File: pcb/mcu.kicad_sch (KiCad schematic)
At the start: 33 parts, among them J1 Conn_01x02_Pin, SW2 SW_Push, U1 TLV1117LV33DCYR, U2 W25Q64JVSSIQ_C179171, U3 STM32H750VBTx, Y1 25 MHz

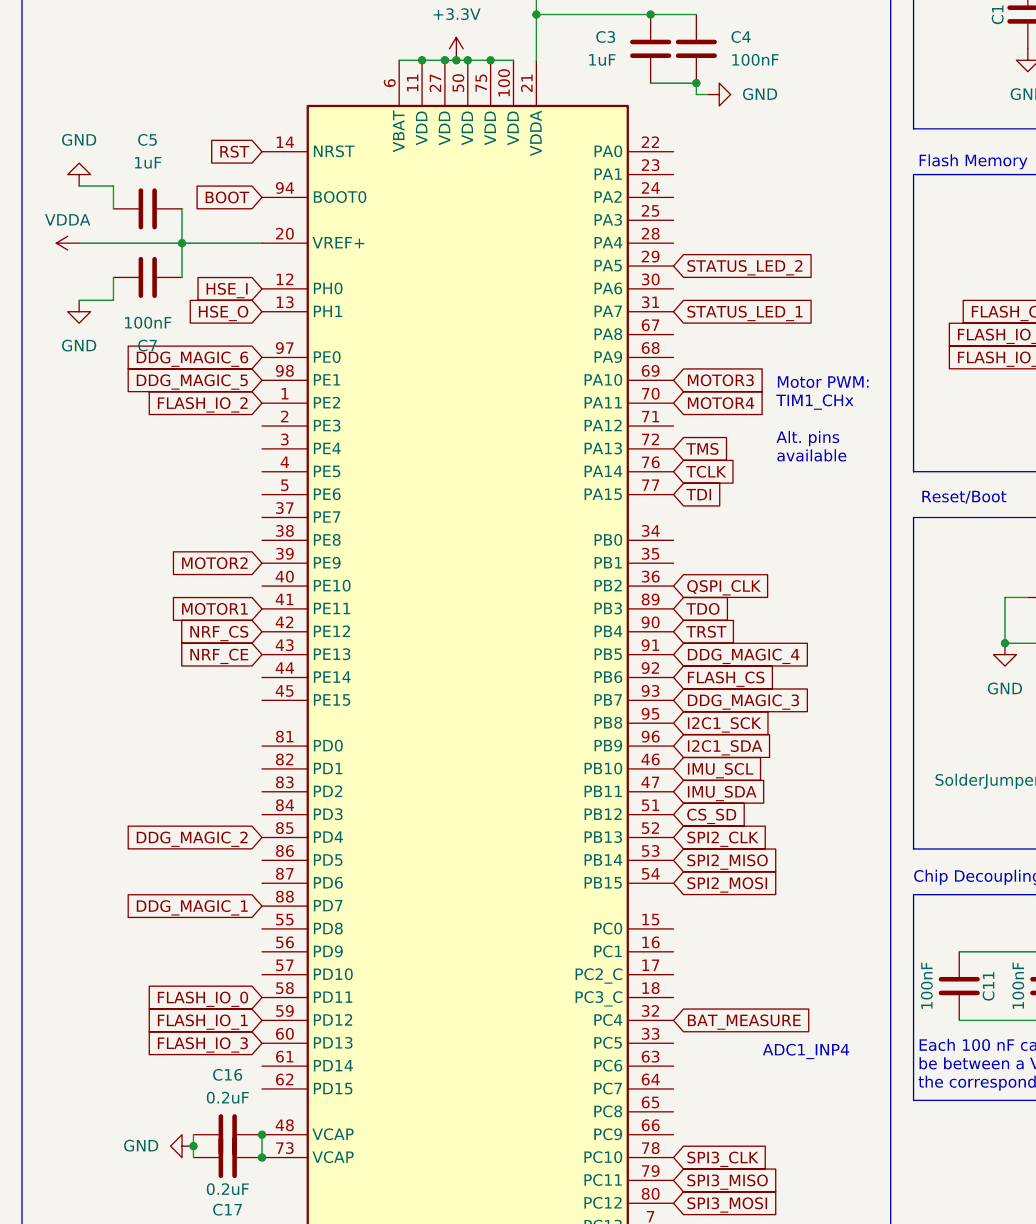
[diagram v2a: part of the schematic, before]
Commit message: [pcb] utilize unused gpios, silkscreen improvements and [journal] add entry for 7/9
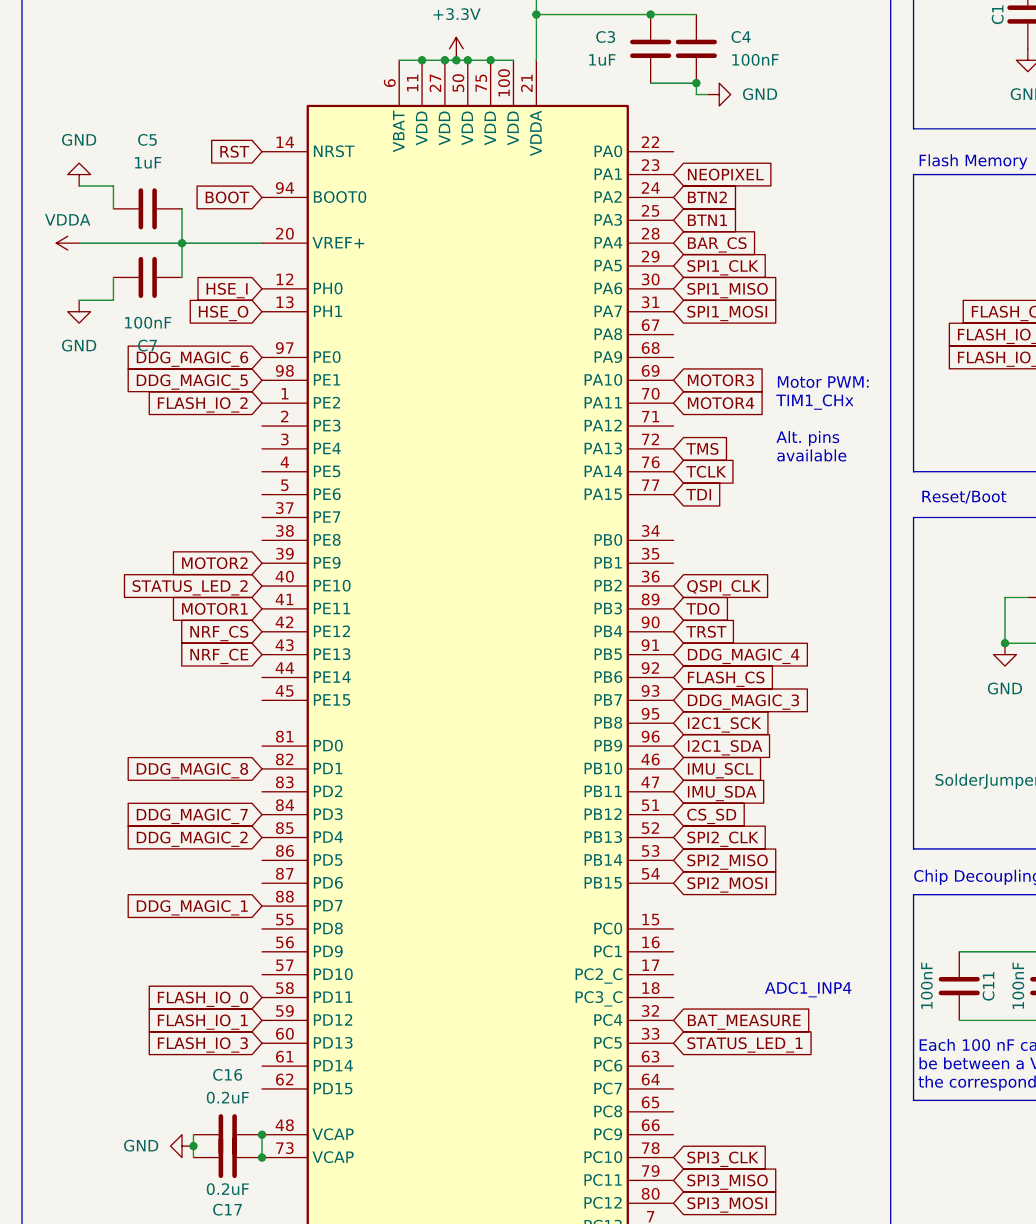
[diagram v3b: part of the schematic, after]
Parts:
- SW2: footprint Button_Switch_THT:SW_PUSH_6mm -> lcsc:SW-SMD_L4.0-W2.9-LS5.0
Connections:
- net STATUS_LED_1: now also U3.33 (PC5); no longer U3.31 (PA7)
- net STATUS_LED_2: now also U3.40 (PE10); no longer U3.29 (PA5)
- net NEOPIXEL: now reaches U3.23 (PA1)
- net BTN2: now reaches U3.24 (PA2)
- net BTN1: now reaches U3.25 (PA3)
- net BAR_CS: now reaches U3.28 (PA4)
- net SPI1_MISO: now reaches U3.30 (PA6)
- net DDG_MAGIC_8: now reaches U3.82 (PD1)
- net DDG_MAGIC_7: now reaches U3.84 (PD3)
- new net SPI1_CLK: U3.29 (PA5)
- new net SPI1_MOSI: U3.31 (PA7)
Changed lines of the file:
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@@
 	(text "ADC1_INP4"
 		(exclude_from_sim no)
-		(at 97.536 145.796 0)
+		(at 97.79 138.938 0)
 		(effects
 			(font
@@
 		)
 	)
+	(global_label "SPI1_CLK"
+		(shape input)
+		(at 87.63 58.42 0)
+		(fields_autoplaced yes)
+		(effects
+			(font
+				(size 1.27 1.27)
+			)
+			(justify left)
+		)
+		(property "Intersheetrefs" "${INTERSHEET_REFS}"
+			(at 99.4447 58.42 0)
+			(effects
+				(font
+					(size 1.27 1.27)
+				)
+				(justify left)
+				(hide yes)
+			)
+		)
+	)
 	(global_label "I2C1_SDA"
 		(shape input)
@@
 		)
 	)
+	(global_label "STATUS_LED_2"
+		(shape input)
+		(at 41.91 93.98 180)
+		(fields_autoplaced yes)
+		(effects
+			(font
+				(size 1.27 1.27)
+			)
+			(justify right)
+		)
+		(property "Intersheetrefs" "${INTERSHEET_REFS}"
+			(at 25.5597 93.98 0)
+			(effects
+				(font
+					(size 1.27 1.27)
+				)
+				(justify right)
+				(hide yes)
+			)
+		)
+	)
 	(global_label "TMS"
 		(shape input)
@@
 		)
 	)
+	(global_label "BAR_CS"
+		(shape input)
+		(at 87.63 55.88 0)
+		(fields_autoplaced yes)
+		(effects
+			(font
+				(size 1.27 1.27)
+			)
+			(justify left)
+		)
+		(property "Intersheetrefs" "${INTERSHEET_REFS}"
+			(at 97.6909 55.88 0)
+			(effects
+				(font
+					(size 1.27 1.27)
+				)
+				(justify left)
+				(hide yes)
+			)
+		)
+	)
 	(global_label "HSE_O"
 		(shape input)
@@
 		)
 	)
+	(global_label "SPI1_MISO"
+		(shape input)
+		(at 87.63 60.96 0)
+		(fields_autoplaced yes)
+		(effects
+			(font
+				(size 1.27 1.27)
+			)
+			(justify left)
+		)
+		(property "Intersheetrefs" "${INTERSHEET_REFS}"
+			(at 100.4728 60.96 0)
+			(effects
+				(font
+					(size 1.27 1.27)
+				)
+				(justify left)
+				(hide yes)
+			)
+		)
+	)
 	(global_label "SPI2_CLK"
 		(shape input)
@@
 		)
 	)
+	(global_label "STATUS_LED_1"
+		(shape input)
+		(at 87.63 144.78 0)
+		(fields_autoplaced yes)
+		(effects
+			(font
+				(size 1.27 1.27)
+			)
+			(justify left)
+		)
+		(property "Intersheetrefs" "${INTERSHEET_REFS}"
+			(at 103.9803 144.78 0)
+			(effects
+				(font
+					(size 1.27 1.27)
+				)
+				(justify left)
+				(hide yes)
+			)
+		)
+	)
 	(global_label "SPI3_MISO"
 		(shape input)
@@
 		)
 	)
-	(global_label "STATUS_LED_1"
+	(global_label "BTN2"
 		(shape input)
-		(at 87.63 63.5 0)
+		(at 87.63 50.8 0)
 		(fields_autoplaced yes)
 		(effects
@@
 		)
 		(property "Intersheetrefs" "${INTERSHEET_REFS}"
-			(at 103.9803 63.5 0)
+			(at 95.3928 50.8 0)
+			(effects
+				(font
+					(size 1.27 1.27)
+				)
+				(justify left)
+				(hide yes)
+			)
+		)
+	)
+	(global_label "NEOPIXEL"
+		(shape input)
+		(at 87.63 48.26 0)
+		(fields_autoplaced yes)
+		(effects
+			(font
+				(size 1.27 1.27)
+			)
+			(justify left)
+		)
+		(property "Intersheetrefs" "${INTERSHEET_REFS}"
+			(at 99.6866 48.26 0)
 			(effects
 				(font
@@
 		)
 	)
+	(global_label "DDG_MAGIC_8"
+		(shape input)
+		(at 41.91 114.3 180)
+		(fields_autoplaced yes)
+		(effects
+			(font
+				(size 1.27 1.27)
+			)
+			(justify right)
+		)
+		(property "Intersheetrefs" "${INTERSHEET_REFS}"
+			(at 26.2853 114.3 0)
+			(effects
+				(font
+					(size 1.27 1.27)
+				)
+				(justify right)
+				(hide yes)
+			)
+		)
+	)
 	(global_label "RST"
 		(shape input)
@@
 		)
 	)
-	(global_label "STATUS_LED_2"
+	(global_label "DDG_MAGIC_7"
 		(shape input)
-		(at 87.63 58.42 0)
+		(at 41.91 119.38 180)
+		(fields_autoplaced yes)
+		(effects
+			(font
+				(size 1.27 1.27)
+			)
+			(justify right)
+		)
+		(property "Intersheetrefs" "${INTERSHEET_REFS}"
+			(at 26.2853 119.38 0)
+			(effects
+				(font
+					(size 1.27 1.27)
+				)
+				(justify right)
+				(hide yes)
+			)
+		)
+	)
+	(global_label "SPI1_MOSI"
+		(shape input)
+		(at 87.63 63.5 0)
 		(fields_autoplaced yes)
 		(effects
@@
 		)
 		(property "Intersheetrefs" "${INTERSHEET_REFS}"
-			(at 103.9803 58.42 0)
+			(at 100.4728 63.5 0)
 			(effects
 				(font
@@
 		)
 	)
+	(global_label "BTN1"
+		(shape input)
+		(at 87.63 53.34 0)
+		(fields_autoplaced yes)
+		(effects
+			(font
+				(size 1.27 1.27)
+			)
+			(justify left)
+		)
+		(property "Intersheetrefs" "${INTERSHEET_REFS}"
+			(at 95.3928 53.34 0)
+			(effects
+				(font
+					(size 1.27 1.27)
+				)
+				(justify left)
+				(hide yes)
+			)
+		)
+	)
 	(global_label "I2C1_SCK"
 		(shape input)
@@
 			)
 		)
-		(property "Footprint" "Button_Switch_THT:SW_PUSH_6mm"
+		(property "Footprint" "lcsc:SW-SMD_L4.0-W2.9-LS5.0"
 			(at 132.08 90.17 0)
 			(effects
@@
 		(on_board yes)
 		(dnp no)
-		(fields_autoplaced yes)
 		(property "Reference" "U3"
 			(at 69.4533 177.8 0)

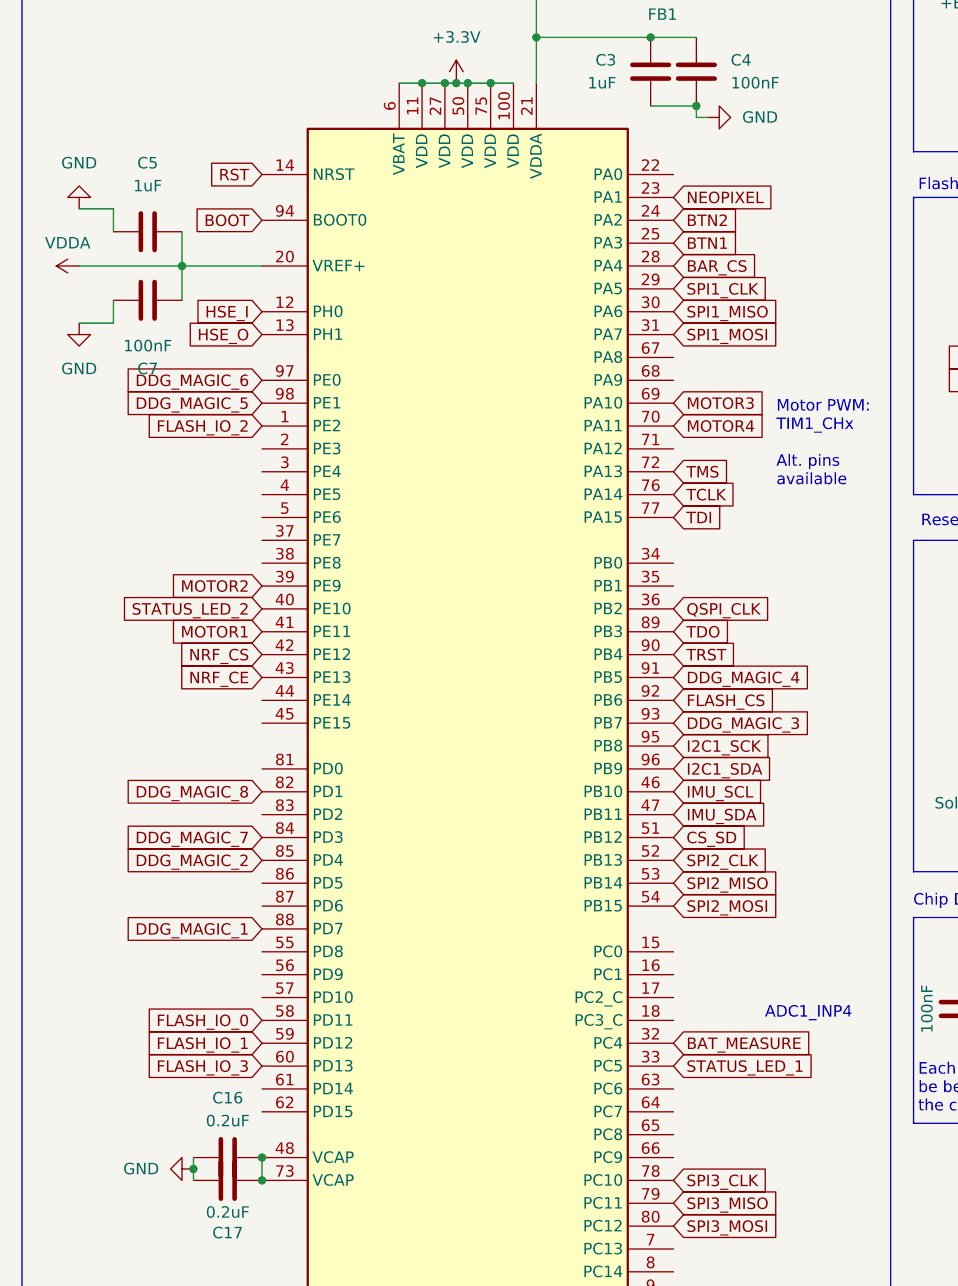
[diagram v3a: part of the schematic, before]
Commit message: [pcb] switch bmi270 to SPI, wire interrupt pins and SD chip detect
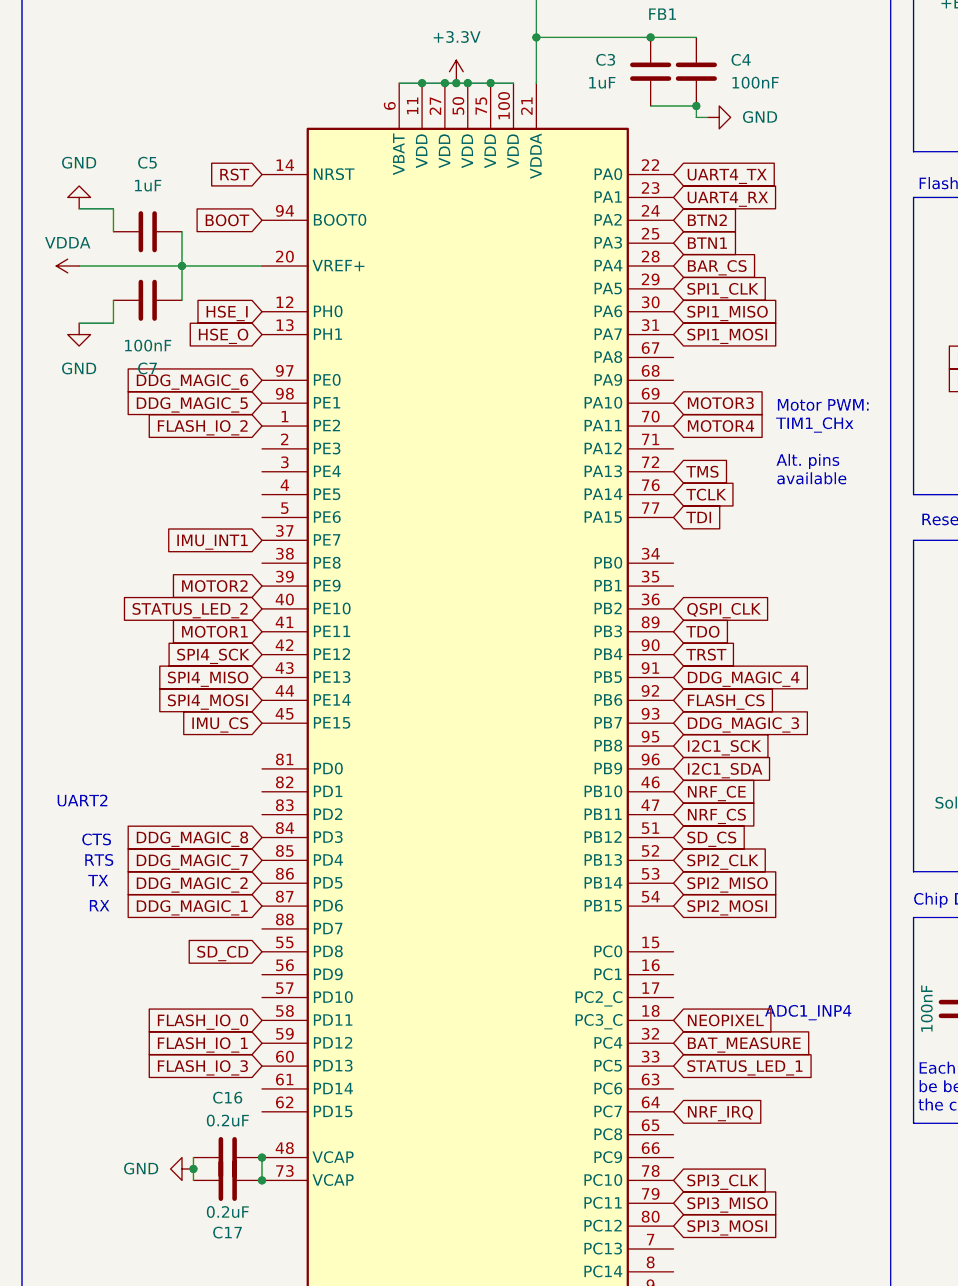
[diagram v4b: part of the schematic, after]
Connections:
- net IMU_SCL is gone; now on net NRF_CE: U3.46 (PB10)
- net IMU_SDA is gone; now on net NRF_CS: U3.47 (PB11)
- net DDG_MAGIC_1: now also U3.87 (PD6); no longer U3.88 (PD7)
- net DDG_MAGIC_2: now also U3.86 (PD5); no longer U3.85 (PD4)
- net DDG_MAGIC_7: now also U3.85 (PD4); no longer U3.84 (PD3)
- net DDG_MAGIC_8: now also U3.84 (PD3); no longer U3.82 (PD1)
- net NEOPIXEL: now also U3.18 (PC3_C); no longer U3.23 (PA1)
- net NRF_CE: no longer U3.43 (PE13)
- net NRF_CS: no longer U3.42 (PE12)
- net UART4_TX: now reaches U3.22 (PA0)
- net IMU_INT1: now reaches U3.37 (PE7)
- net SPI4_MOSI: now reaches U3.44 (PE14)
- net IMU_CS: now reaches U3.45 (PE15)
- net SD_CD: now reaches U3.55 (PD8)
- net NRF_IRQ: now reaches U3.64 (PC7)
- net CS_SD renamed SD_CS
- new net SPI4_MISO: U3.43 (PE13)
- new net SPI4_SCK: U3.42 (PE12)
- new net UART4_RX: U3.23 (PA1)
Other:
- note added: "CTS"
- note added: "RTS"
- note added: "RX"
- note added: "TX"
- note added: "UART2"

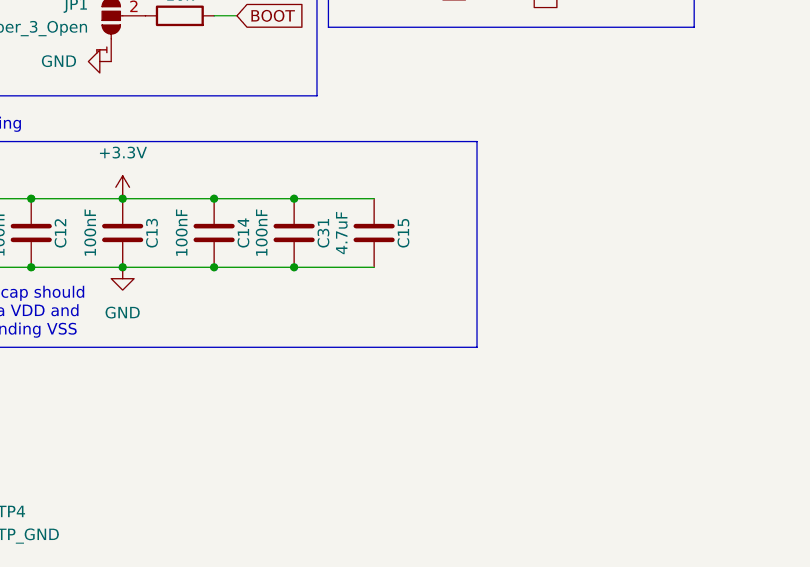
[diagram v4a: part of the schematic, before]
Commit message: [pcb] various routing improvements
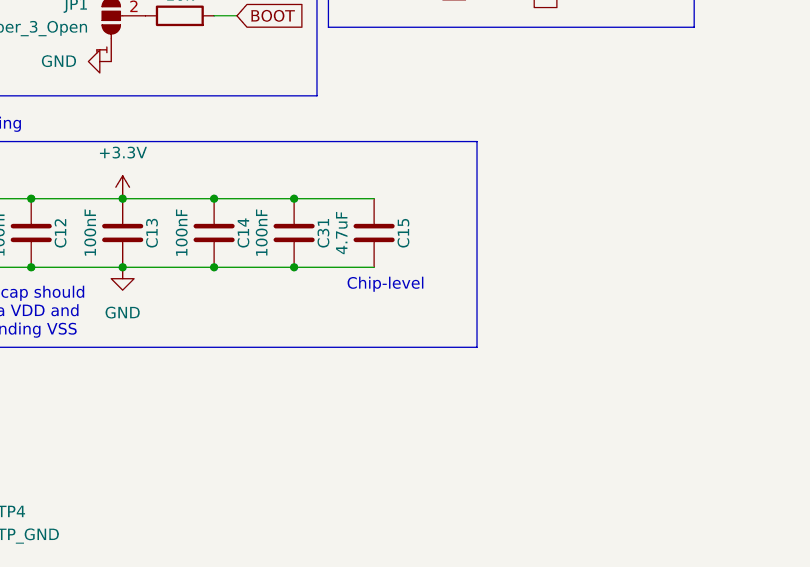
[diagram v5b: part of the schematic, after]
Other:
- note added: "Chip-level"
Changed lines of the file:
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@@
+		)
+	)
+	(text "Chip-level"
+		(exclude_from_sim no)
+		(at 164.592 144.272 0)
+		(effects
+			(font
+				(size 1.27 1.27)
+				(color 194 0 194 1)
+			)
+			(justify left)
 		)
 	)
